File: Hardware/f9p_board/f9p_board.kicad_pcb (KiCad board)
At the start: 2 copper layers, 50 x 30 mm, 59 parts, among them J1 USB_B_Mini, J2 USB_B_Mini, J4 CAN, J5 Active Antenna, P1 SWD, SW1 F9P_USB_POWER, U1 Ublox_ZED_F9P, U2 STM32F405RGTx, U3 MCP16311MS, U4 ncv8705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

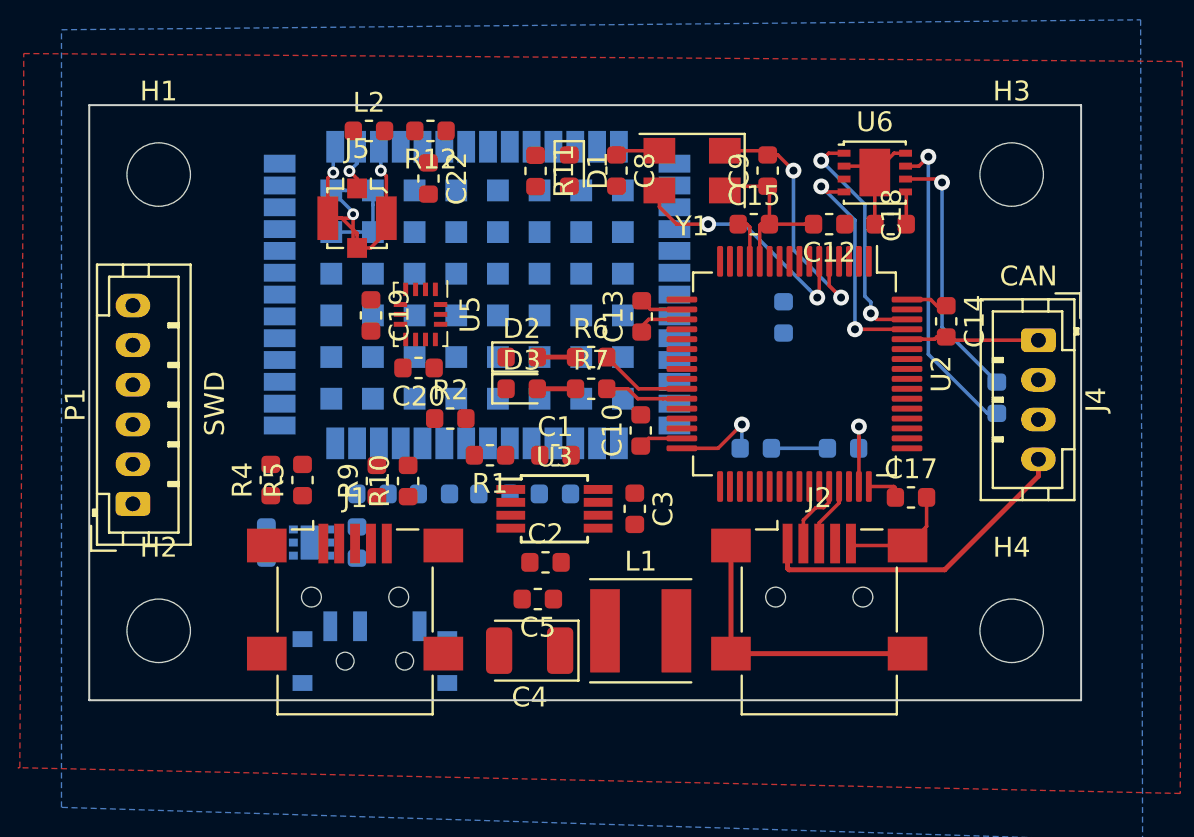
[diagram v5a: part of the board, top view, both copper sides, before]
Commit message: f9p_board: Routed everything, needs review
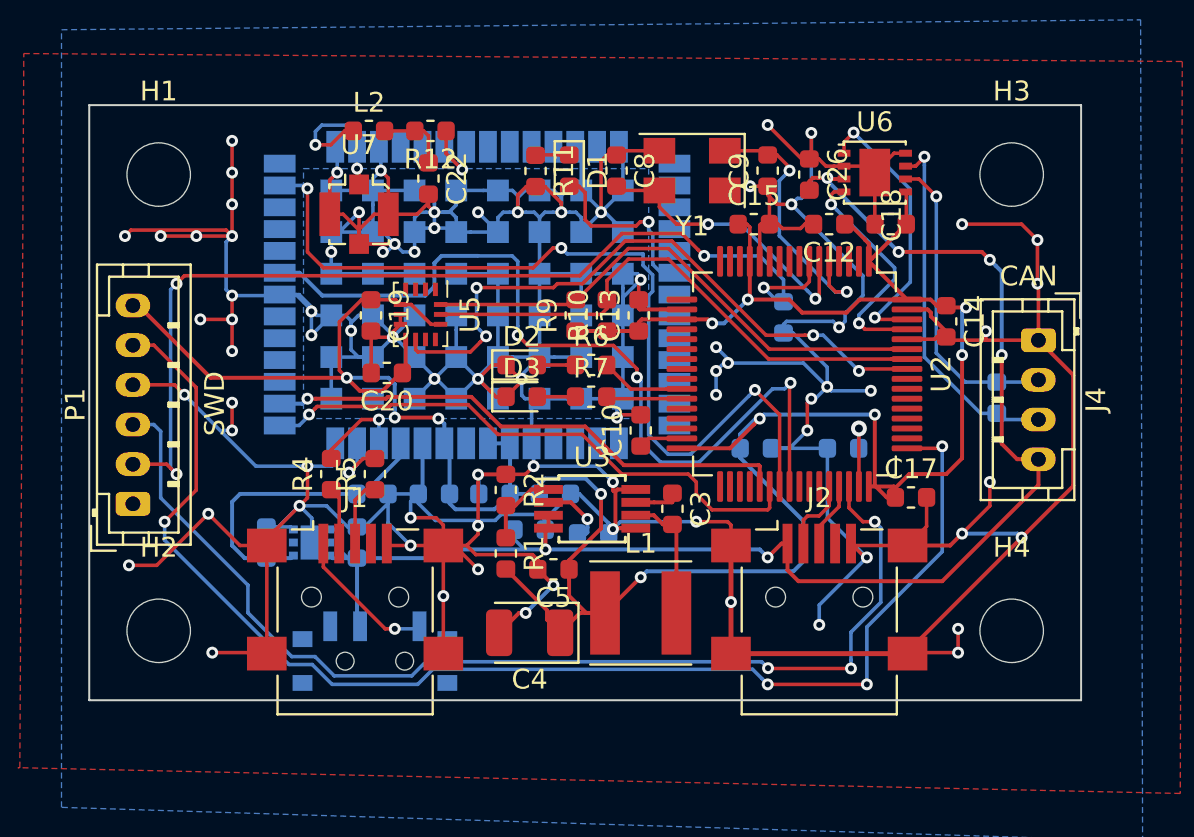
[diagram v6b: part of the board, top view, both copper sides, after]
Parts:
- removed J5: Active Antenna, Connector_Coaxial:U.FL_Molex_MCRF_73412-0110_Vertical
- added C26: 2.2u, Capacitor_SMD:C_0603_1608Metric, F.Cu at (106.3, 63.5)
- added U7: uFL_conn, Connector_Coaxial:U.FL_Molex_MCRF_73412-0110_Vertical, F.Cu at (83.6, 65.5)
- C1, C2: moved to B.Cu
- moved R9 13.0 mm to (94.5, 70.6)
- moved R10 13.0 mm to (96.1, 70.6)
- moved R1 5.01 mm to (91.0, 82.6), turned to -90 degrees
- moved R2 4.56 mm to (91.0, 79.4), turned to -90 degrees
- moved C1 3.97 mm to (92.2, 81.4)
- moved R5 3.66 mm to (84.4, 78.6)
- moved R4 3.06 mm to (82.2, 78.6)
- moved C2 2.80 mm to (95.4, 81.6)
- moved C3 1.90 mm to (99.4, 80.3)
- moved U3 1.90 mm to (95.3, 80.3)
- moved C5 1.69 mm to (93.4, 83.4)
- moved C20 1.62 mm to (85.0, 73.5)
- moved C4 0.90 mm to (92.2, 86.6)
- moved L1 0.90 mm to (97.8, 85.6)
- moved D3 0.40 mm to (91.8, 74.7)
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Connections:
- U4 pad GND: (no net) -> GND
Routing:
- net GND: track 74.8 -> 484.3 mm, vias 3 -> 78
- net VCC: track 15.2 -> 152.6 mm, vias 1 -> 11
- net SWCLK: track 0.00 -> 66.9 mm, vias 0 -> 4
- net MCU_USB_VBUS: track 16.7 -> 74.3 mm, vias 0 -> 6
- net SWDIO: track 0.00 -> 55.5 mm, vias 0 -> 3
- net NRST: track 0.00 -> 50.7 mm, vias 0 -> 4
- net TIMEPULSE: track 0.00 -> 44.3 mm, vias 0 -> 3
- net F9P_RESET_N: track 0.00 -> 43.2 mm, vias 0 -> 3
- net IMU_INT2: track 0.00 -> 32.5 mm, vias 0 -> 4
- net MCU_RX_F9P_TX: track 0.00 -> 28.8 mm, vias 0 -> 1
- net SCL: track 0.00 -> 27.6 mm
- net MCU_TX_F9P_RX: track 0.00 -> 26.8 mm, vias 0 -> 1
- net SDA: track 0.00 -> 26.8 mm
- net F9P_3v3: track 0.00 -> 15.7 mm
- net Net-(D1-Pad2): track 0.00 -> 9.22 mm, vias 0 -> 1
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
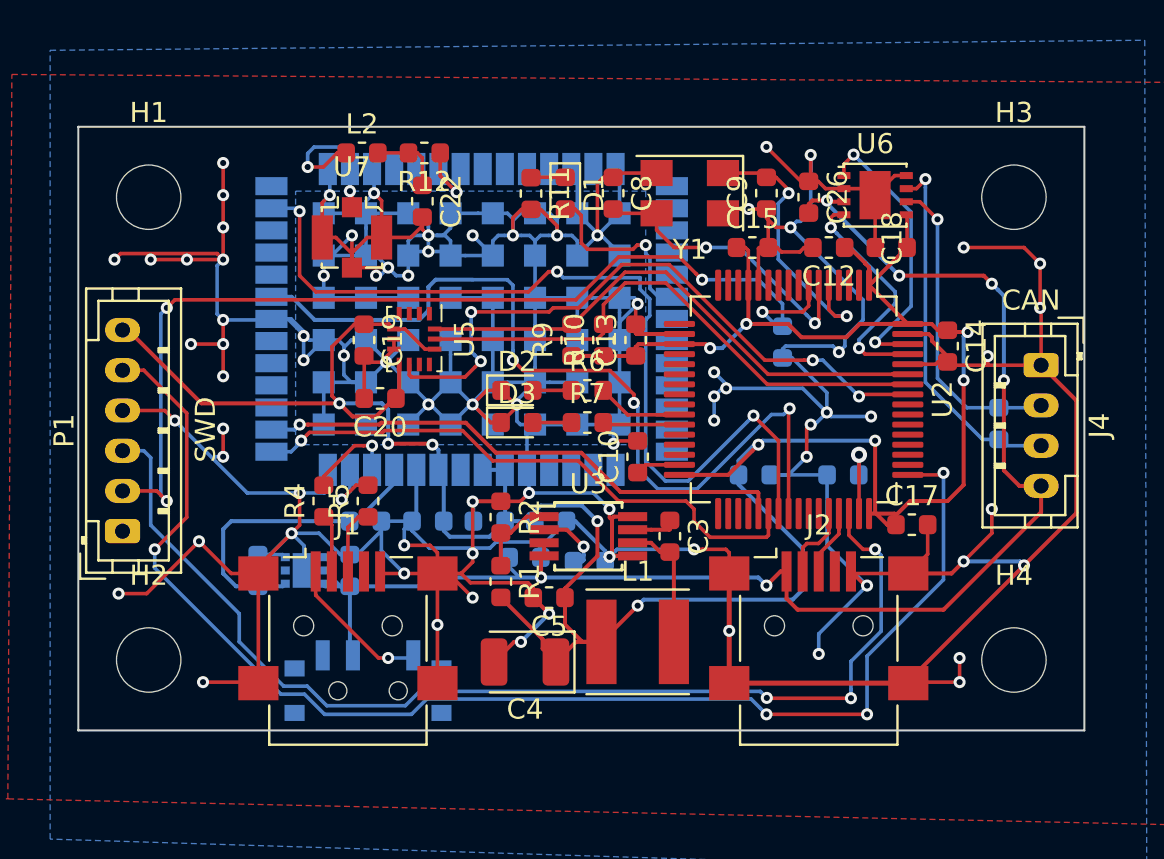
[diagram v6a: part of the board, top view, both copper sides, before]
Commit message: F9P_Board moving silks text around and adding resistors on USB data +/- lines
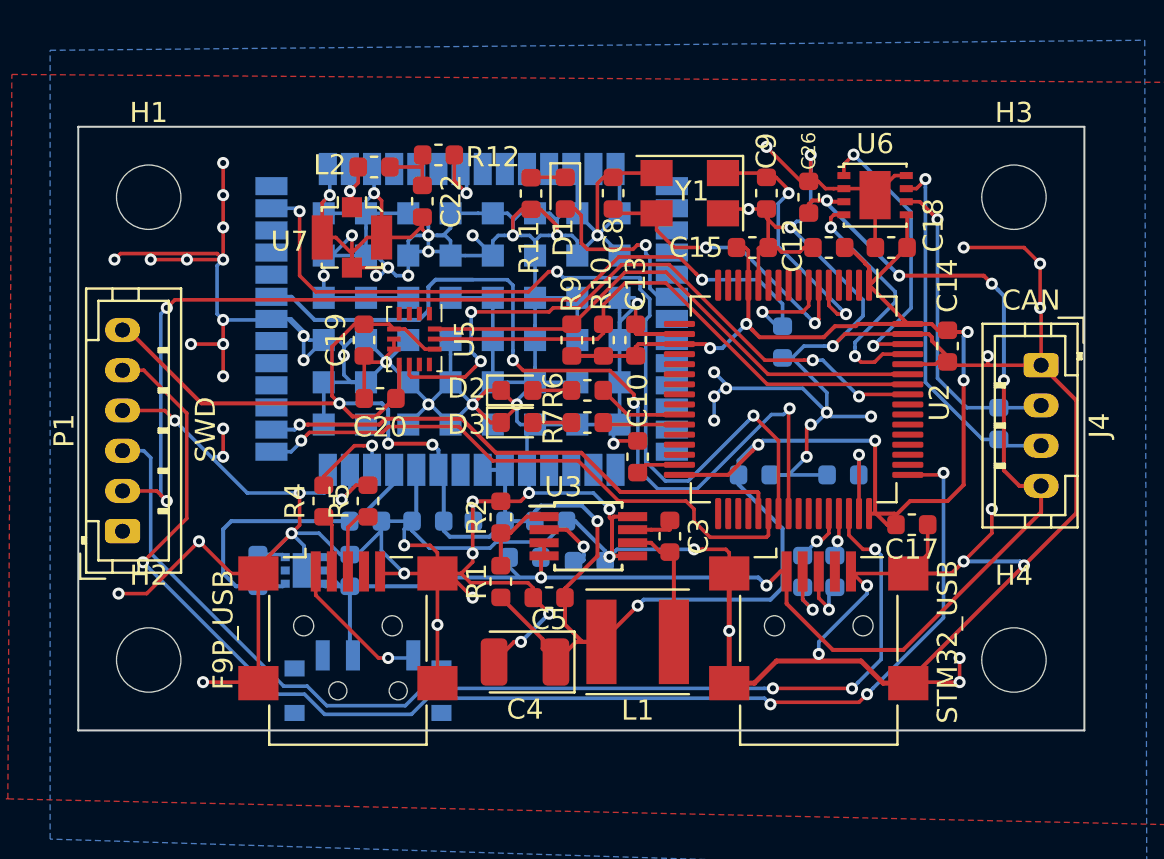
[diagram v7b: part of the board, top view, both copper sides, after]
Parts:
- added R13: 27 Ohm, Resistor_SMD:R_0603_1608Metric, B.Cu at (106.0, 82.1)
- added R14: 27 Ohm, Resistor_SMD:R_0603_1608Metric, B.Cu at (107.6, 82.1)
- moved L2 0.92 mm to (84.7, 62.0)
- moved R12 0.71 mm to (87.9, 61.4)
- renumbered U1 to F9P, J1 to F9P_USB, J2 to STM32_USB, SW1 to USB_PWR
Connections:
- U2 pad 44: MCU_USB_DM -> Net-(R13-Pad2)
- U2 pad 45: MCU_USB_DP -> Net-(R14-Pad2)
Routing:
- net Net-(L2-Pad1): track 8.07 -> 3.31 mm, vias 2 -> 1
- net GND: track 484.3 -> 481.6 mm
- net Net-(R13-Pad2): track 0.00 -> 2.74 mm, vias 0 -> 1
- net Net-(R14-Pad2): track 0.00 -> 2.17 mm, vias 0 -> 1
- net MCU_USB_VBUS: track 74.3 -> 76.1 mm
- net VCC: track 152.6 -> 151.2 mm
- net CAN_RX: track 11.8 -> 12.7 mm
- net Net-(C9-Pad2): track 14.1 -> 13.4 mm
- net SWDIO: track 55.5 -> 54.9 mm
- net MCU_USB_DM: track 3.75 -> 3.43 mm, vias 0 -> 1
- net MCU_USB_DP: track 3.29 -> 3.34 mm, vias 0 -> 1
- added copper zone on B.Cu, net (none)
- removed copper zone on B.Cu, net GND

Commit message: Some updates on F9P board
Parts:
- removed STM32_USB: USB_B_Mini, Connector_USB:USB_Mini-B_Lumberg_2486_01_Horizontal
- added J2: USB_B_Mini, Connector_USB:USB_Mini-B_Lumberg_2486_01_Horizontal, F.Cu at (106.8, 84.8)
- renumbered F9P_USB to J1, USB_PWR to SW1, F9P to U1
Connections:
- U5 pad 1: Net-(U5-Pad1) -> GND
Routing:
- net GND: track 481.6 -> 486.7 mm, vias 78 -> 79
- added copper zone on B.Cu, net GND
- removed copper zone on B.Cu, net (none)
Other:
- net class Default: via_dia 0.8 -> 0.6; via_drill 0.4 -> 0.3
- rule pad_to_mask_clearance: 0.051 -> 0.01
- board text added: "OFF"
- board text added: "ON"
